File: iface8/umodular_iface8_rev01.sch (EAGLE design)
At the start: 39 parts, among them U4 SN74HC165DR, U6 SN74HC595D

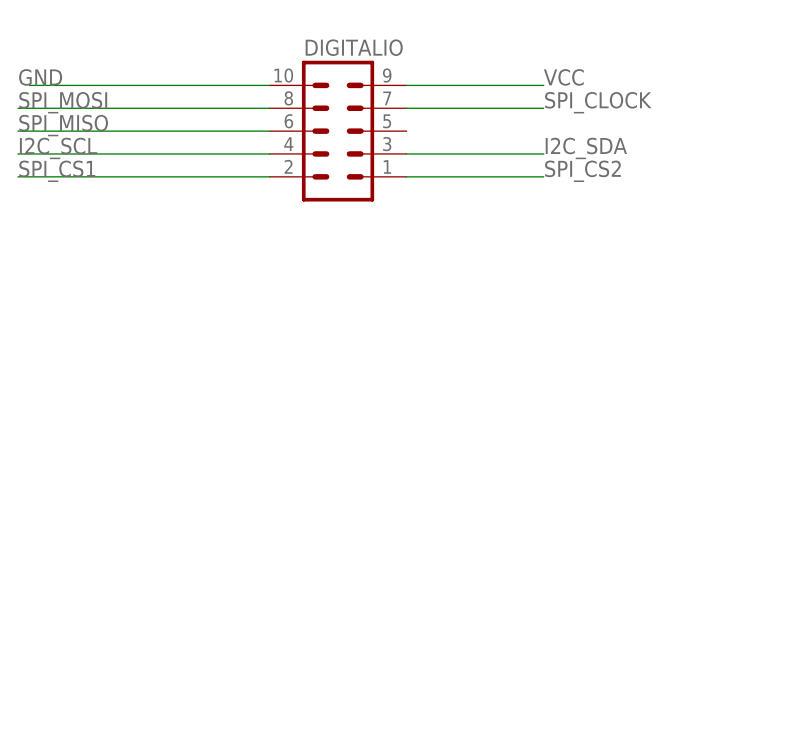
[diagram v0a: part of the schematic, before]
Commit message: iface8: align components.
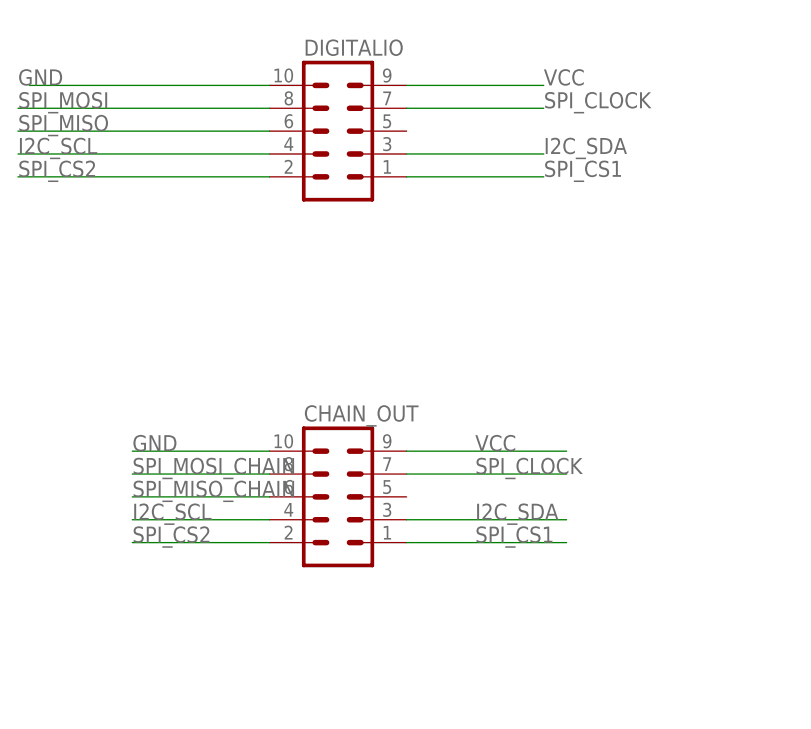
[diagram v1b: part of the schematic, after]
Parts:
- added CHAIN_OUT: (no value), con-lstb:MA05-2
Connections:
- net GND: now also CHAIN_OUT.10
- net I2C_SCL: now also CHAIN_OUT.4
- net I2C_SDA: now also CHAIN_OUT.3
- net SPI_CLOCK: now also CHAIN_OUT.7
- net SPI_CS1: now also CHAIN_OUT.1, DIGITALIO.1; no longer DIGITALIO.2
- net SPI_CS2: now also CHAIN_OUT.2, DIGITALIO.2; no longer DIGITALIO.1
- net SPI_MISO_CHAIN: now also CHAIN_OUT.6
- net SPI_MOSI_CHAIN: now also CHAIN_OUT.8
- net VCC: now also CHAIN_OUT.9
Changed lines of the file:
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@@
 <part name="R20" library="Seeed-Resistor-2016" deviceset="SMD-RES-220R-5%-1/10W(0603)" device="" value="220R"/>
 <part name="C6" library="Seeed-Capacitor-2016" deviceset="CERAMIC-100NF-50V-10%-X7R(0805)" device="" value="100nf"/>
+<part name="CHAIN_OUT" library="con-lstb" deviceset="MA05-2" device=""/>
 </parts>
 <sheets>
@@
 <instance part="R20" gate="G$1" x="129.54" y="30.48"/>
 <instance part="C6" gate="G$1" x="76.2" y="60.96" rot="R90"/>
+<instance part="CHAIN_OUT" gate="G$1" x="45.72" y="195.58"/>
 </instances>
 <busses>
@@
 <wire x1="129.54" y1="238.76" x2="109.22" y2="238.76" width="0.1524" layer="91"/>
 <label x="109.22" y="238.76" size="1.778" layer="95"/>
+</segment>
+<segment>
+<pinref part="CHAIN_OUT" gate="G$1" pin="10"/>
+<wire x1="38.1" y1="200.66" x2="22.86" y2="200.66" width="0.1524" layer="91"/>
+<label x="22.86" y="200.66" size="1.778" layer="95"/>
 </segment>
 </net>
@@
 <label x="109.22" y="241.3" size="1.778" layer="95"/>
 </segment>
+<segment>
+<pinref part="CHAIN_OUT" gate="G$1" pin="9"/>
+<wire x1="53.34" y1="200.66" x2="71.12" y2="200.66" width="0.1524" layer="91"/>
+<label x="60.96" y="200.66" size="1.778" layer="95"/>
+</segment>
 </net>
 <net name="SPI_CLOCK" class="0">
@@
 <label x="25.4" y="45.72" size="1.778" layer="95"/>
 </segment>
+<segment>
+<pinref part="CHAIN_OUT" gate="G$1" pin="7"/>
+<wire x1="53.34" y1="198.12" x2="71.12" y2="198.12" width="0.1524" layer="91"/>
+<label x="60.96" y="198.12" size="1.778" layer="95"/>
+</segment>
 </net>
 <net name="SPI_MISO" class="0">
@@
 </segment>
 <segment>
-<pinref part="DIGITALIO" gate="G$1" pin="2"/>
-<wire x1="38.1" y1="231.14" x2="10.16" y2="231.14" width="0.1524" layer="91"/>
-<label x="10.16" y="231.14" size="1.778" layer="95"/>
+<pinref part="CHAIN_OUT" gate="G$1" pin="1"/>
+<wire x1="53.34" y1="190.5" x2="71.12" y2="190.5" width="0.1524" layer="91"/>
+<label x="60.96" y="190.5" size="1.778" layer="95"/>
+</segment>
+<segment>
+<pinref part="DIGITALIO" gate="G$1" pin="1"/>
+<wire x1="53.34" y1="231.14" x2="68.58" y2="231.14" width="0.1524" layer="91"/>
+<label x="68.58" y="231.14" size="1.778" layer="95"/>
 </segment>
 </net>
@@
 <wire x1="30.48" y1="133.35" x2="30.48" y2="142.24" width="0.1524" layer="91"/>
 </segment>
+<segment>
+<pinref part="CHAIN_OUT" gate="G$1" pin="6"/>
+<wire x1="38.1" y1="195.58" x2="22.86" y2="195.58" width="0.1524" layer="91"/>
+<label x="22.86" y="195.58" size="1.778" layer="95"/>
+</segment>
 </net>
 <net name="SPI_CS2" class="0">
@@
 </segment>
 <segment>
-<pinref part="DIGITALIO" gate="G$1" pin="1"/>
-<wire x1="53.34" y1="231.14" x2="68.58" y2="231.14" width="0.1524" layer="91"/>
-<label x="68.58" y="231.14" size="1.778" layer="95"/>
+<pinref part="CHAIN_OUT" gate="G$1" pin="2"/>
+<wire x1="38.1" y1="190.5" x2="22.86" y2="190.5" width="0.1524" layer="91"/>
+<label x="22.86" y="190.5" size="1.778" layer="95"/>
+</segment>
+<segment>
+<pinref part="DIGITALIO" gate="G$1" pin="2"/>
+<wire x1="38.1" y1="231.14" x2="10.16" y2="231.14" width="0.1524" layer="91"/>
+<label x="10.16" y="231.14" size="1.778" layer="95"/>
 </segment>
 </net>
@@
 <label x="88.9" y="27.94" size="1.778" layer="95"/>
 </segment>
+<segment>
+<pinref part="CHAIN_OUT" gate="G$1" pin="8"/>
+<wire x1="38.1" y1="198.12" x2="22.86" y2="198.12" width="0.1524" layer="91"/>
+<label x="22.86" y="198.12" size="1.778" layer="95"/>
+</segment>
 </net>
 <net name="N$2" class="0">
@@
 <label x="109.22" y="236.22" size="1.778" layer="95"/>
 </segment>
+<segment>
+<pinref part="CHAIN_OUT" gate="G$1" pin="4"/>
+<wire x1="38.1" y1="193.04" x2="22.86" y2="193.04" width="0.1524" layer="91"/>
+<label x="22.86" y="193.04" size="1.778" layer="95"/>
+</segment>
 </net>
 <net name="I2C_SDA" class="0">
@@
 <label x="109.22" y="233.68" size="1.778" layer="95"/>
 </segment>
-</net>
+<segment>
+<pinref part="CHAIN_OUT" gate="G$1" pin="3"/>
+<wire x1="53.34" y1="193.04" x2="71.12" y2="193.04" width="0.1524" layer="91"/>
+<label x="60.96" y="193.04" size="1.778" layer="95"/>
+</segment>
+</net>

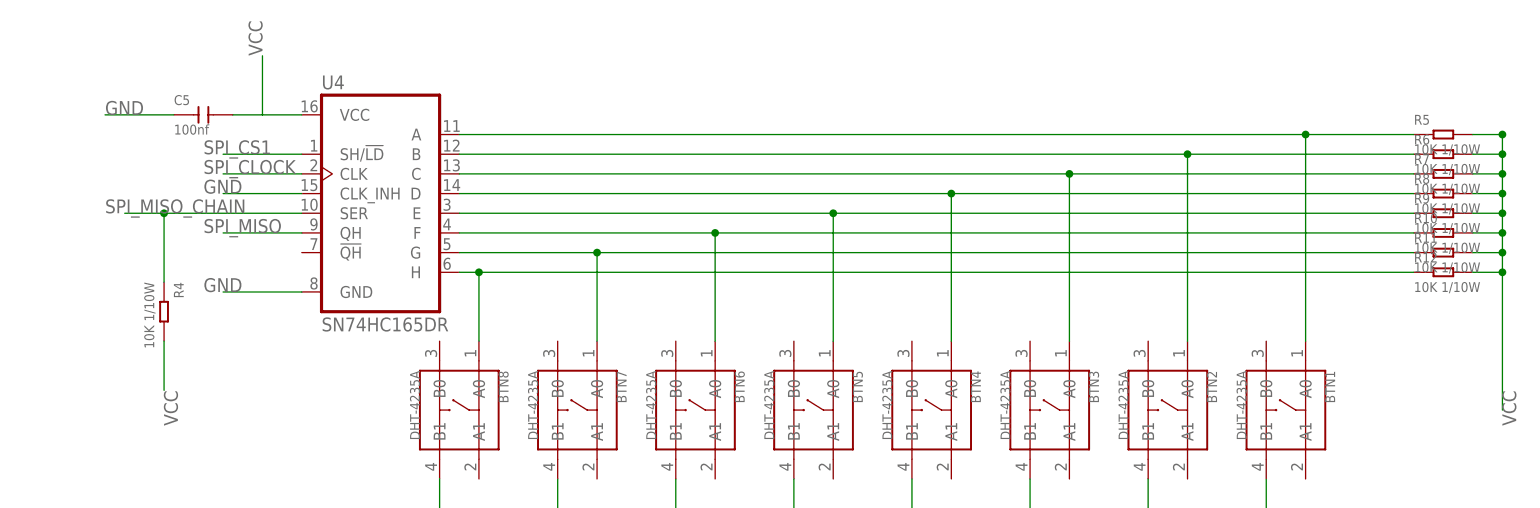
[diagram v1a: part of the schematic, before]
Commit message: iface8: ready to route boy!
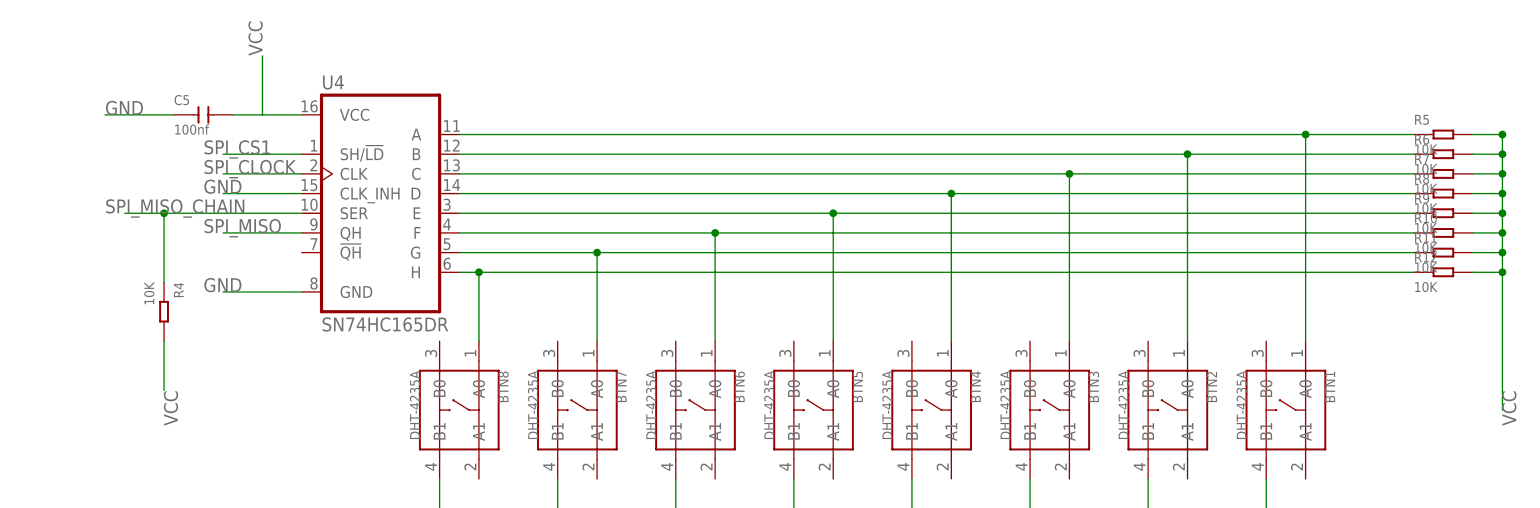
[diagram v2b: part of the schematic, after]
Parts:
- R10, R11, R12, R4, R5, R6, R7, R8, R9: value 10K 1/10W -> 10K
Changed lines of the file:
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@@
 <part name="BTN7" library="Seeed-Switch-2016" deviceset="SMD-BUTTON-TOP-DHT-4235A(4P-4.2X3.2MM)" device="" value="DHT-4235A"/>
 <part name="BTN8" library="Seeed-Switch-2016" deviceset="SMD-BUTTON-TOP-DHT-4235A(4P-4.2X3.2MM)" device="" value="DHT-4235A"/>
-<part name="R6" library="Seeed-Resistor-2016" deviceset="SMD-RES-10K-5%-1/10W(0603)" device="" value="10K 1/10W"/>
-<part name="R7" library="Seeed-Resistor-2016" deviceset="SMD-RES-10K-5%-1/10W(0603)" device="" value="10K 1/10W"/>
-<part name="R8" library="Seeed-Resistor-2016" deviceset="SMD-RES-10K-5%-1/10W(0603)" device="" value="10K 1/10W"/>
-<part name="R9" library="Seeed-Resistor-2016" deviceset="SMD-RES-10K-5%-1/10W(0603)" device="" value="10K 1/10W"/>
-<part name="R10" library="Seeed-Resistor-2016" deviceset="SMD-RES-10K-5%-1/10W(0603)" device="" value="10K 1/10W"/>
-<part name="R11" library="Seeed-Resistor-2016" deviceset="SMD-RES-10K-5%-1/10W(0603)" device="" value="10K 1/10W"/>
-<part name="R12" library="Seeed-Resistor-2016" deviceset="SMD-RES-10K-5%-1/10W(0603)" device="" value="10K 1/10W"/>
-<part name="R5" library="Seeed-Resistor-2016" deviceset="SMD-RES-10K-5%-1/10W(0603)" device="" value="10K 1/10W"/>
+<part name="R6" library="Seeed-Resistor-2016" deviceset="SMD-RES-10K-5%-1/10W(0603)" device="" value="10K"/>
+<part name="R7" library="Seeed-Resistor-2016" deviceset="SMD-RES-10K-5%-1/10W(0603)" device="" value="10K"/>
+<part name="R8" library="Seeed-Resistor-2016" deviceset="SMD-RES-10K-5%-1/10W(0603)" device="" value="10K"/>
+<part name="R9" library="Seeed-Resistor-2016" deviceset="SMD-RES-10K-5%-1/10W(0603)" device="" value="10K"/>
+<part name="R10" library="Seeed-Resistor-2016" deviceset="SMD-RES-10K-5%-1/10W(0603)" device="" value="10K"/>
+<part name="R11" library="Seeed-Resistor-2016" deviceset="SMD-RES-10K-5%-1/10W(0603)" device="" value="10K"/>
+<part name="R12" library="Seeed-Resistor-2016" deviceset="SMD-RES-10K-5%-1/10W(0603)" device="" value="10K"/>
+<part name="R5" library="Seeed-Resistor-2016" deviceset="SMD-RES-10K-5%-1/10W(0603)" device="" value="10K"/>
 <part name="C5" library="Seeed-Capacitor-2016" deviceset="CERAMIC-100NF-50V-10%-X7R(0805)" device="" value="100nf"/>
-<part name="R4" library="Seeed-Resistor-2016" deviceset="SMD-RES-10K-5%-1/10W(0603)" device="" value="10K 1/10W"/>
+<part name="R4" library="Seeed-Resistor-2016" deviceset="SMD-RES-10K-5%-1/10W(0603)" device="" value="10K"/>
 <part name="BTN2" library="Seeed-Switch-2016" deviceset="SMD-BUTTON-TOP-DHT-4235A(4P-4.2X3.2MM)" device="" value="DHT-4235A"/>
 <part name="BTN3" library="Seeed-Switch-2016" deviceset="SMD-BUTTON-TOP-DHT-4235A(4P-4.2X3.2MM)" device="" value="DHT-4235A"/>
